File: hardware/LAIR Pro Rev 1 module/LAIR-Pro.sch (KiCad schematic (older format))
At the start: 11 parts, among them J1 Conn_02x10_Odd_Even, J2 Conn_02x10_Odd_Even, J3 Conn_02x10_Odd_Even, J4 Conn_02x10_Odd_Even, J5 RC2014_Pro_Bus, J6 RC2014_Pro_Bus, J7 Conn_02x05_Odd_Even, U1 74LS240, U2 74LS244

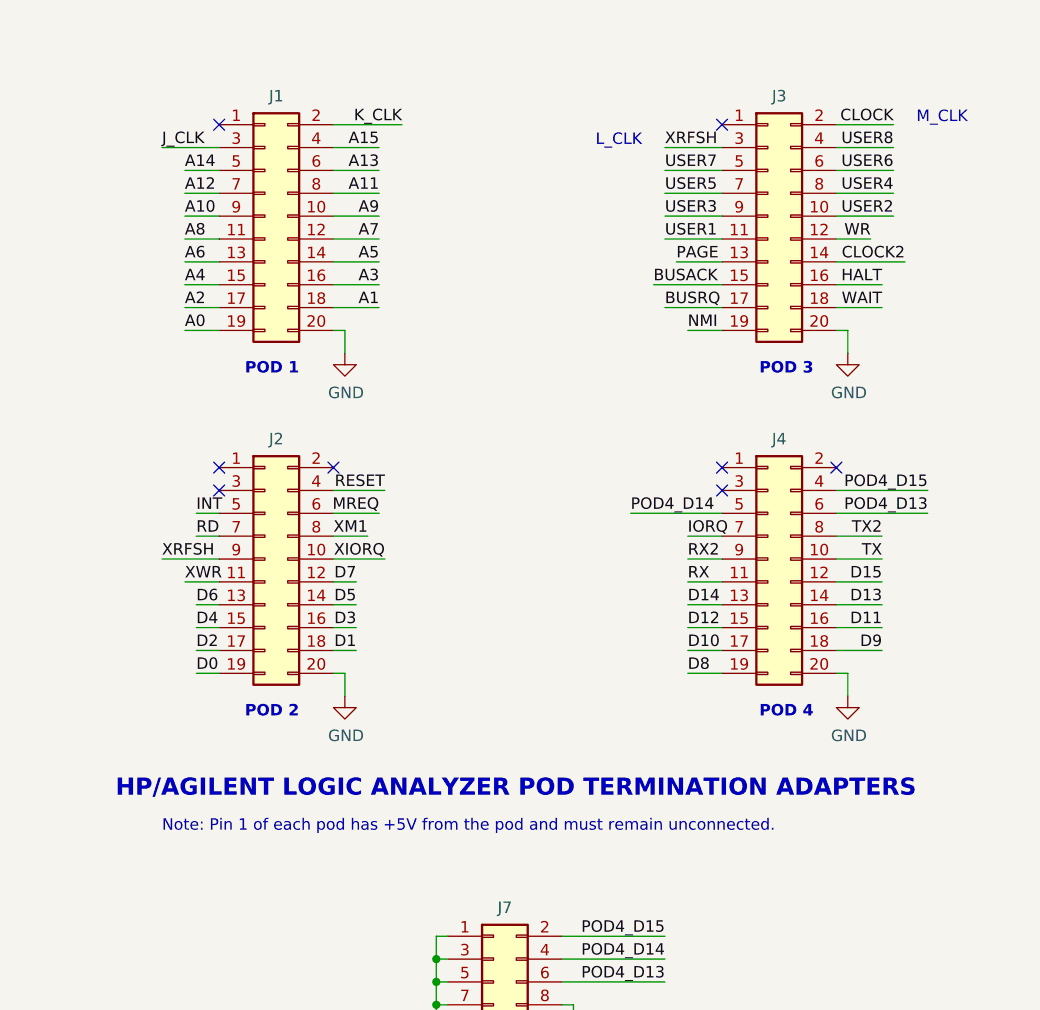
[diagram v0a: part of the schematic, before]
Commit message: Use only one clock input per pod
The documentation for the HP Termination Adapter calls out
two clock signals on each adapter, but the actual pods on
the logic analyzers have only one clock per pod, which is
on pin3 of the Termination Adapter. Pin 2 is unused.
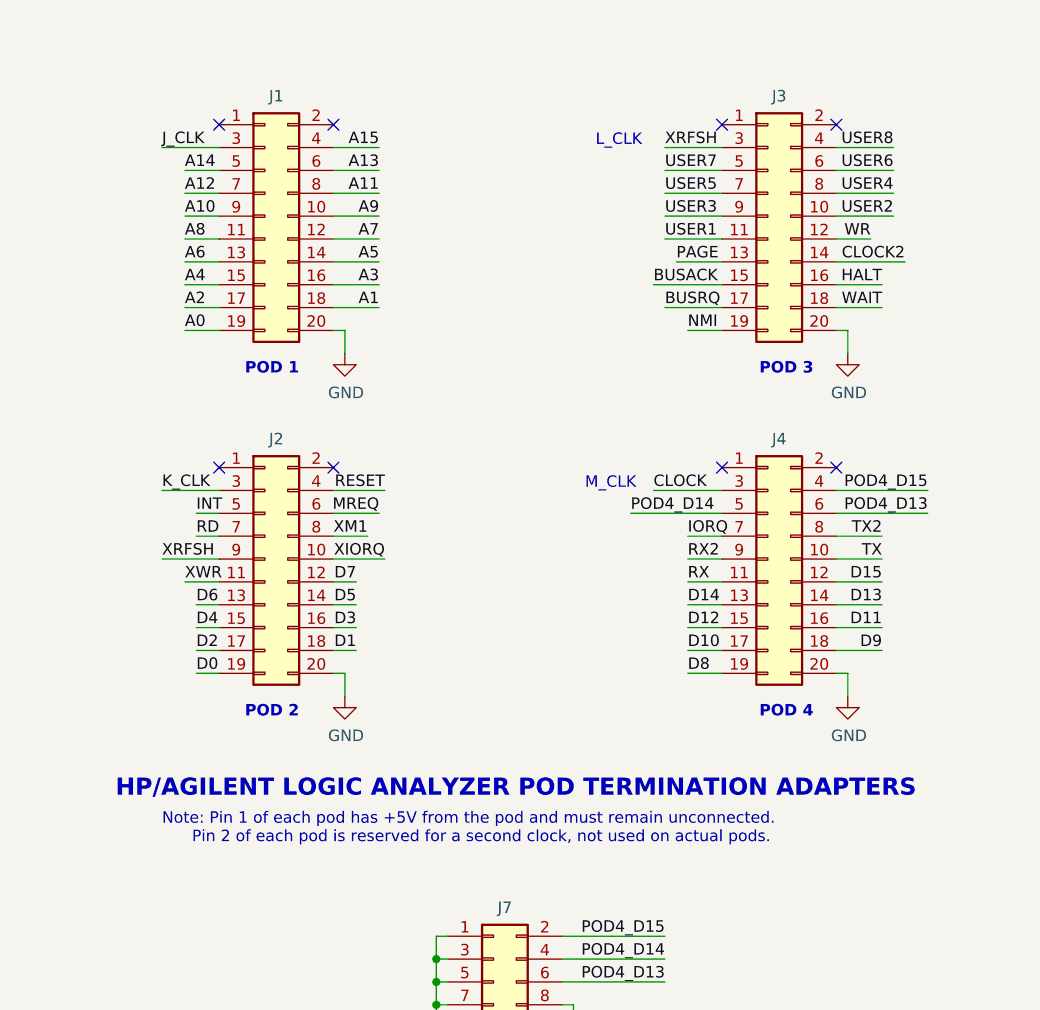
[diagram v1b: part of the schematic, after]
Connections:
- net CLOCK: now also J4.3 (Pin_3); no longer J3.2 (Pin_2)
- net K_CLK: now also J2.3 (Pin_3); no longer J1.2 (Pin_2)
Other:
- note added: "Note: Pin 1 of each pod has +5V from the pod and must remain unconnected.\n Pin 2 of each pod is reserved for a second clock, not used on actual pods."
- note removed: "Note: Pin 1 of each pod has +5V from the pod and must remain unconnected."
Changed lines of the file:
@@
 Sheet 1 1
 Title "LAIR-Pro Logic Analyzer Interface for RC2014 Pro Bus"
-Date "2019-06-21"
+Date "2019-07-03"
 Rev "Rev1"
 Comp "Must Be Art"
@@
 Text Label 9650 3150 2    50   ~ 0
 D15
-Text Label 7550 1150 2    50   ~ 0
-K_CLK
-Wire Wire Line
-	7550 1150 7250 1150
 Text Label 6500 3050 0    50   ~ 0
 XRFSH
@@
 	9700 1550 9450 1550
 NoConn ~ 9450 2650
-NoConn ~ 8950 2750
 Text Label 8800 3150 0    50   ~ 0
 RX
@@
 Text Notes 1650 7900 0    50   ~ 0
 As specified for STAT symbol used by Z80 inverse assembler
-NoConn ~ 6750 2750
 NoConn ~ 7250 2650
-Text Label 9700 1150 2    50   ~ 0
-CLOCK
 Text Label 8700 1250 0    50   ~ 0
 XRFSH
 Wire Wire Line
-	9450 1150 9700 1150
-Wire Wire Line
 	8950 2950 8800 2950
 Wire Wire Line
@@
 Wire Wire Line
 	7250 3050 7475 3050
-Text Notes 6500 4250 0    50   ~ 0
-Note: Pin 1 of each pod has +5V from the pod and must remain unconnected.
+Text Notes 6500 4300 0    50   ~ 0
+Note: Pin 1 of each pod has +5V from the pod and must remain unconnected.\n      Pin 2 of each pod is reserved for a second clock, not used on actual pods.
 $Comp
 L 74xx:74LS240 U1
@@
 Wire Wire Line
 	3350 2700 3800 2700
-Text Notes 9800 1150 0    50   ~ 0
+Text Notes 8350 2750 0    50   ~ 0
 M_CLK
 Text Notes 8600 1250 2    50   ~ 0
 L_CLK
+Text Label 8650 2750 0    50   ~ 0
+CLOCK
+Wire Wire Line
+	8650 2750 8950 2750
+NoConn ~ 9450 1150
+Text Label 6500 2750 0    50   ~ 0
+K_CLK
+Wire Wire Line
+	6750 2750 6500 2750
+NoConn ~ 7250 1150
 $EndSCHEMATC

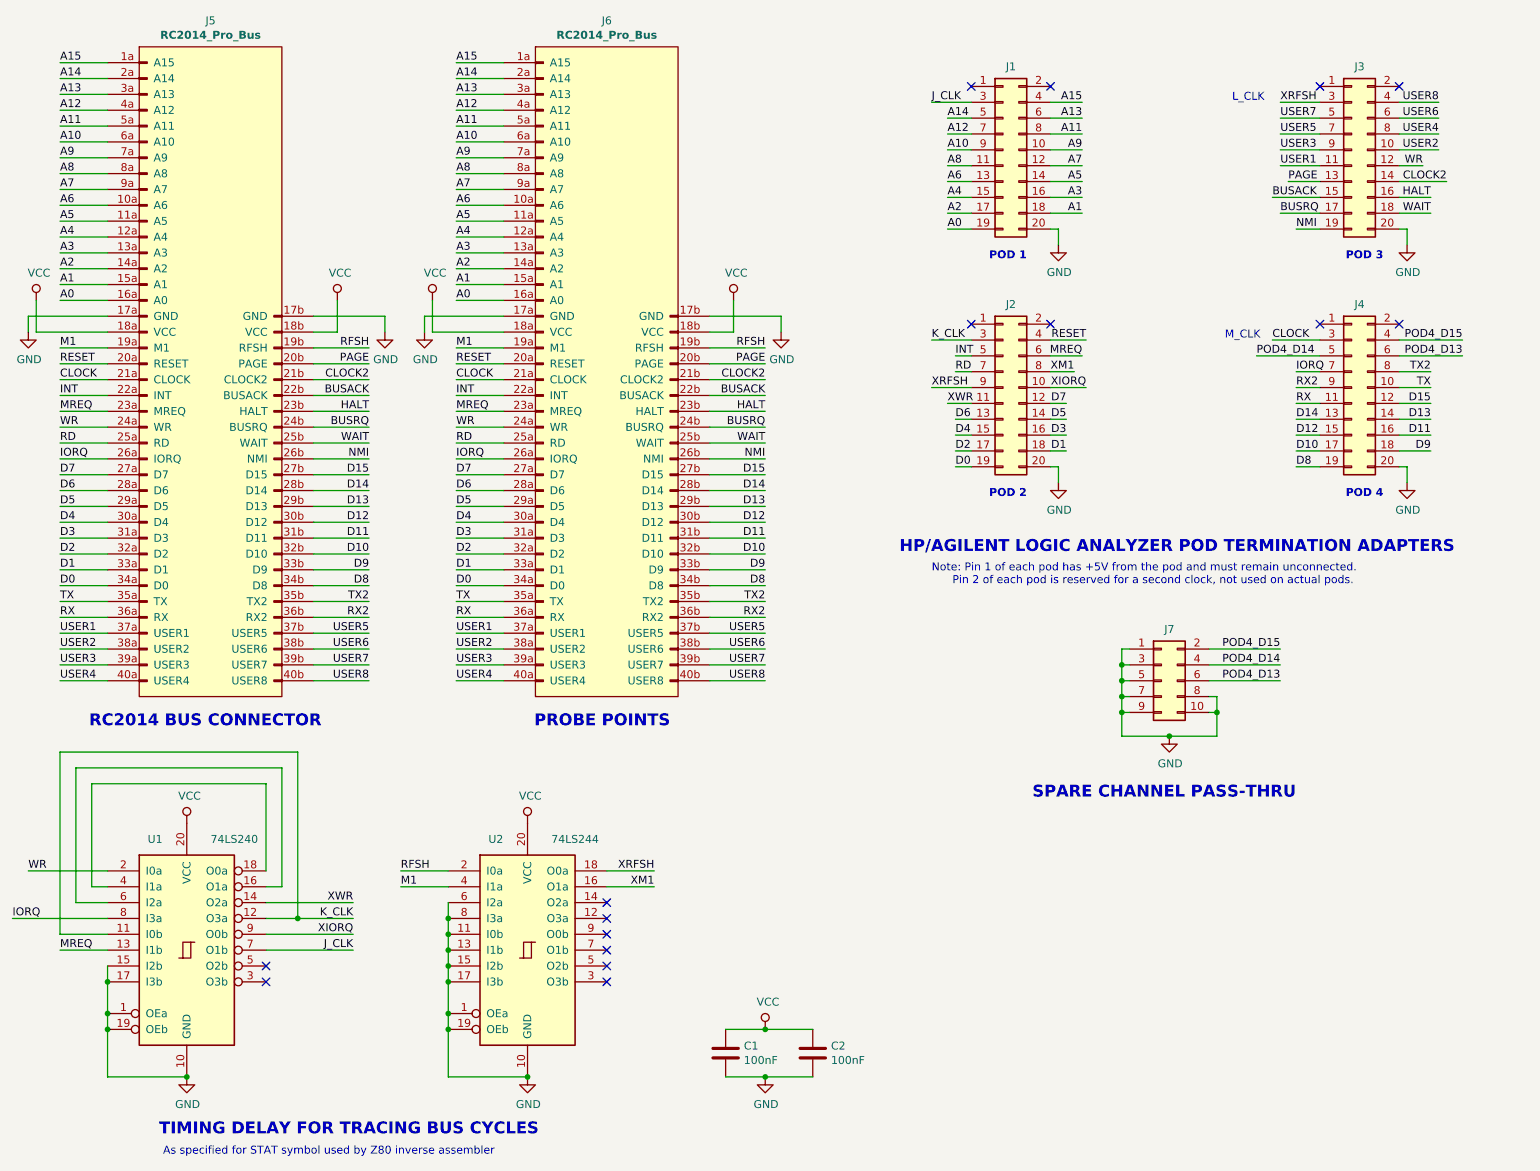
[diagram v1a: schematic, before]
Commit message: Adjust timing to account for HP's buffering everything
On the HP Z80 adapter, they buffer the address bus, the data bus,
and every other signal through a 74LS241. They then have to add
more delay to WR and IORQ to make the timing work, and for some
reason they invert WR while they're at it.

We don't have room to buffer everything, so we can't follow HP's
design without expanding the board beyond the RC-2014 form factor.
Since we aren't buffering ADDR or DATA, we can't add delays to
the other control signals, either. We just need to add the extra
delays on WR and IORQ. We keep WR inverted for compatibility.

The HP Z80 adapter also inverts IORQ and MREQ for use as the clocks
of the state analyzer. I don't know why. We can't invert them (that
would add unwanted delay), so the user will need to configure the
Master Clock for rising edges on J and K, rather than falling edges
as with the HP adapter.

This change leaves most of U1 and U2 unused. The data sheet says
we need to tie off the unused inputs. They are now tied to ground
through individual visible traces on the back side, so they can
be cut if the gates are needed for mods.
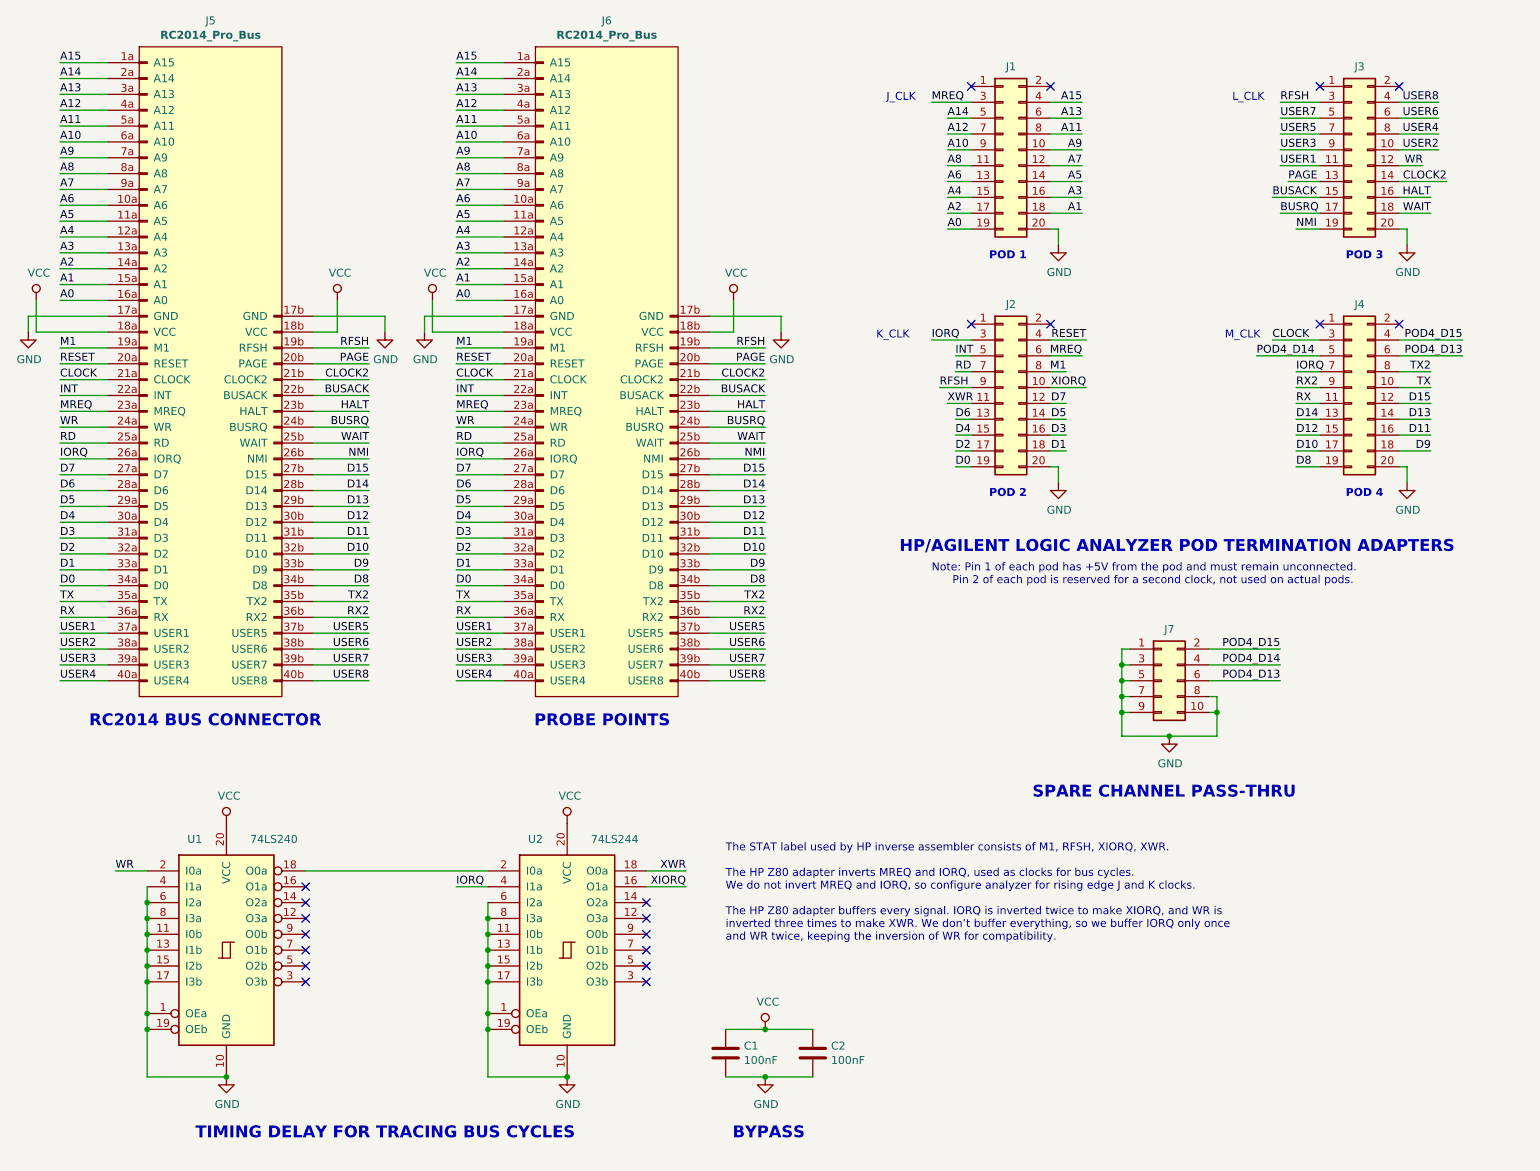
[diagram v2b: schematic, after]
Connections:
- net GND: now also U1.11 (I0b), U1.13 (I1b), U1.4 (I1a), U1.6 (I2a), U1.8 (I3a)
- net IORQ: now also J2.3 (Pin_3), U2.4 (I1a); no longer U1.8 (I3a)
- net M1: now also J2.8 (Pin_8); no longer U2.4 (I1a)
- net MREQ: now also J1.3 (Pin_3); no longer U1.13 (I1b)
- net RFSH: now also J2.9 (Pin_9), J3.3 (Pin_3); no longer U2.2 (I0a)
- net XIORQ: now also U2.16 (O1a); no longer U1.9 (O0b)
- net XWR: now also U2.18 (O0a); no longer U1.14 (O2a)
- net at U1.16 (O1a): no longer U1.6 (I2a)
- net at U1.18 (O0a): now also U2.2 (I0a); no longer U1.4 (I1a)
- net J_CLK: no longer names the net of U1.7 (O1b)
- net J_CLK: no longer J1.3 (Pin_3)
- removed net K_CLK: J2.3 (Pin_3), U1.11 (I0b), U1.12 (O3a)
- removed net XM1: J2.8 (Pin_8), U2.16 (O1a)
- removed net XRFSH: J2.9 (Pin_9), J3.3 (Pin_3), U2.18 (O0a)
- no-connect marks 16 -> 21
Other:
- note added: "BYPASS"
- note added: "J_CLK"
- note added: "K_CLK"
- note added: "The STAT label used by HP inverse assembler consists of M1, RFSH, XIORQ, XWR. \n\nThe HP Z80 adapter inverts MREQ and IORQ, used as clocks for bus cycles.\nWe do not invert MREQ and IORQ, so configure analyzer for rising edge J and K clocks.\n\nThe HP Z80 adapter buffers every signal. IORQ is inverted twice to make XIORQ, and WR is\ninverted three times to make XWR. We don’t buffer everything, so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"
- note removed: "As specified for STAT symbol used by Z80 inverse assembler"
- moved on the sheet: U1, U2
